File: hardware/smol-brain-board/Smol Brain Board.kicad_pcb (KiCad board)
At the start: 2 copper layers, 44.8 x 52.6 mm, 59 parts, among them J1 USB4085-GF-A, J3 CAN_DBG, J6 Smol_Brain_Board, J7 PROGRAM, U1 ESP32-S3-WROOM-1-N8, U3 SN65HVD231D

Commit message: fix: Corrected DRC settings
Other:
- rule pad_to_mask_clearance: 0.1016 -> 0.038

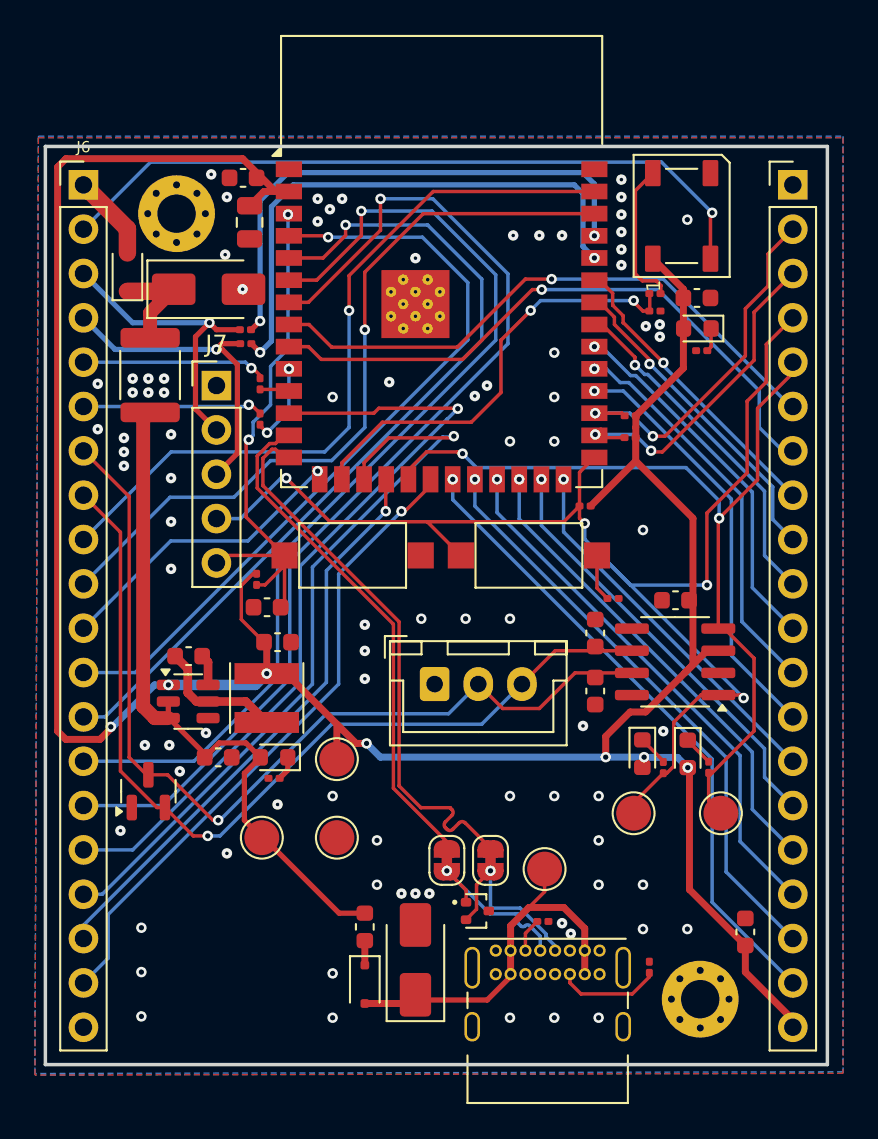
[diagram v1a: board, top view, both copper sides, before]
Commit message: Added real world components and finalised PCB, ready for manufacturing
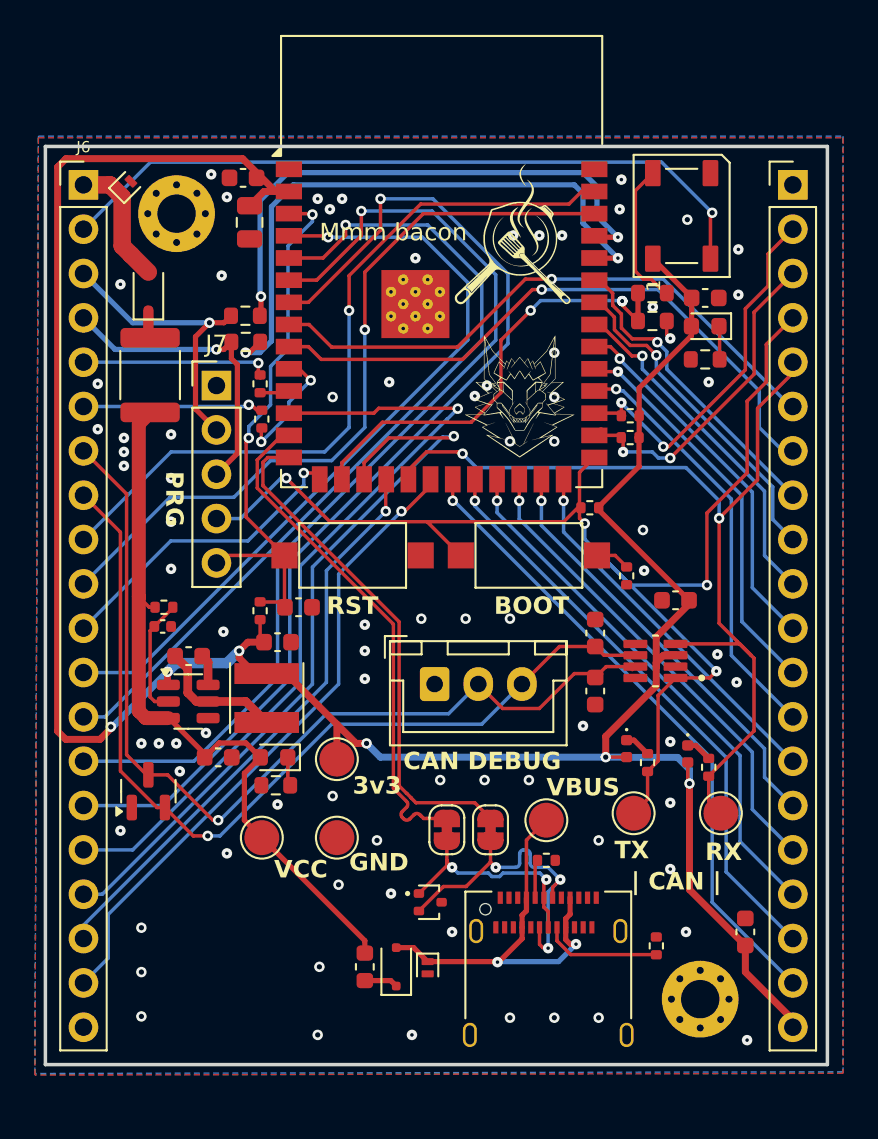
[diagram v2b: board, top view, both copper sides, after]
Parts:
- removed D5: SMBJ26A, Diode_SMD:D_SMA
- removed U3: SN65HVD231D, Package_SO:SOIC-8_3.9x4.9mm_P1.27mm
- added C12: 0.1uF, Capacitor_SMD:C_0402_1005Metric, F.Cu at (132.7, 106.3)
- added D7: PESD1, Diode_SMD:D_SOD-882, F.Cu at (130.7, 81.0)
- added R10: 10k, Resistor_SMD:R_0402_1005Metric, F.Cu at (132.8, 105.2)
- added U2: TCAN3414, Library:TCAN3414, F.Cu at (160.9, 108.3)
- C9: value Capacitor 1u 25V 0603 -> Capacitor 1u 25V
- CRX1, CTX1: footprint LED_SMD:LED_0603_1608Metric -> LED_SMD:LED_0402_1005Metric
- D2: value SMBJ5.0A-TR -> PESD1; footprint Diode_SMD:D_SMA -> Diode_SMD:D_SOD-882
- J1: value USB4085-GF-A -> USB_C_Receptacle; footprint Connector_USB:USB_C_Receptacle_GCT_USB4085 -> Connector_USB:USB_C_Receptacle_Amphenol_12401610E4-2A
- R1, R3: value Resistor 4.7k 0603 -> 4.7k; footprint Resistor_SMD:R_0201_0603Metric -> Resistor_SMD:R_0402_1005Metric
- R12, R14: value Resistor 1k 0603 -> 1k; footprint Resistor_SMD:R_0201_0603Metric -> Resistor_SMD:R_0402_1005Metric
- R13: value Resistor 100R 0603 -> 100R; footprint Resistor_SMD:R_0201_0603Metric -> Resistor_SMD:R_0402_1005Metric
- R15, R16, R5, R7, R8, R9: footprint Resistor_SMD:R_0201_0603Metric -> Resistor_SMD:R_0603_1608Metric
- R17, R18, R19: footprint Resistor_SMD:R_0201_0603Metric -> Resistor_SMD:R_0402_1005Metric
- R2, R4: value Resistor 5.1k 0603 -> Resistor 5.1k; footprint Resistor_SMD:R_0201_0603Metric -> Resistor_SMD:R_0402_1005Metric
- R6: value Resistor 10k 0603 -> 10k; footprint Resistor_SMD:R_0201_0603Metric -> Resistor_SMD:R_0402_1005Metric
- moved J1 3.61 mm to (154.8, 126.9)
- moved R4 3.51 mm to (154.7, 119.7)
- moved VBUS1 2.80 mm to (154.7, 117.4)
- moved D6 2.75 mm to (148.1, 122.1)
- moved F2 2.29 mm to (144.3, 125.8)
- moved D4 2.06 mm to (146.1, 125.8), turned to 90 degrees
- moved R6 1.81 mm to (138.3, 105.4), turned to 90 degrees
- moved C9 1.80 mm to (140.5, 105.2), turned to 0 degrees
- moved JP1 1.75 mm to (149.0, 118.0)
- moved JP2 1.75 mm to (151.5, 118.0)
- moved D1 1.63 mm to (131.9, 87.1)
- moved R13 1.52 mm to (159.3, 103.4), turned to -90 degrees
- moved R2 1.29 mm to (161.0, 124.6)
- moved R12 0.94 mm to (160.5, 114.1)
- moved CTX1 0.94 mm to (159.3, 113.3)
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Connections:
- J1 pad A8: (no net) -> unconnected-(J1-SBU1-PadA8)
- J1 pad B6: (no net) -> /USB_D_P
- J1 pad B7: (no net) -> /USB_D_N
- J1 pad B8: (no net) -> unconnected-(J1-SBU2-PadB8)
- VR1 pad 2: Net-(VIN_IND1-A) -> Net-(VR1-EN)
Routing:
- net /USB_D_N: track 10.4 -> 19.7 mm, vias 1 -> 3
- net Net-(VR1-EN): track 0.00 -> 7.25 mm
- net Net-(D1-K): track 6.04 -> 1.56 mm
- net /CAN_RX: track 51.3 -> 55.6 mm
- net Net-(U1-RXD0): track 31.9 -> 35.0 mm
- net /uC_USB_D_N: track 33.0 -> 30.0 mm
- net 3V3: track 156.6 -> 153.8 mm, vias 7 -> 6
- net /USB_D_P: track 10.4 -> 13.0 mm, vias 1 -> 2
- net VIN: track 4.94 -> 7.43 mm
- net Net-(U1-IO17): track 4.80 -> 7.17 mm
- net Net-(VIN_IND1-A): track 40.0 -> 41.8 mm
- net /CAN_TX: track 78.4 -> 76.7 mm
- net /RST: track 31.1 -> 32.6 mm
- net GND: track 0.00 -> 1.22 mm, vias 85 -> 79
- net VBUS: track 22.5 -> 23.6 mm, vias 0 -> 2
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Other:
- board text added: "BOOT"
- board text added: "CAN DEBUG"
- board text added: "Mmm bacon"
- board text added: "PRG"
- board text added: "RST"
- board text added: "VBUS"
- board text added: "VCC"
- board text added: "| CAN |"

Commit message: Fixed footprint mismatch
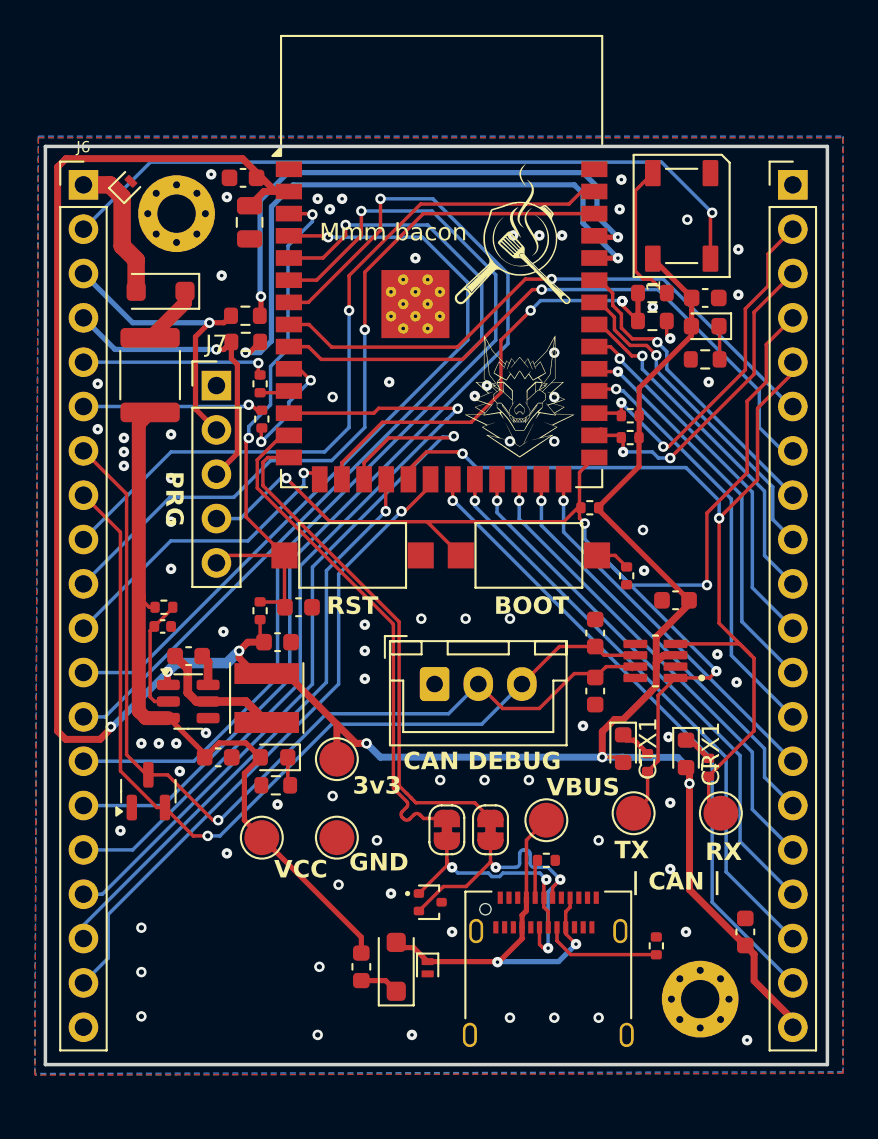
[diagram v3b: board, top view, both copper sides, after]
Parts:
- CRX1, CTX1: footprint LED_SMD:LED_0402_1005Metric -> LED_SMD:LED_0603_1608Metric
- D1, D4: footprint Diode_SMD:D_SOD-323F -> Diode_SMD:D_SOD-123F
- moved D1 0.70 mm to (132.6, 87.1), turned to 180 degrees
- moved CTX1 0.20 mm to (159.1, 113.3)
- moved F2 0.20 mm to (144.1, 125.8)
- moved CRX1 0.10 mm to (162.7, 113.6)
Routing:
- net Net-(D1-K): track 1.56 -> 3.49 mm
- net VIN: track 7.43 -> 8.24 mm
- net GND: vias 79 -> 78
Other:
- rule pad_to_mask_clearance: 0.038 -> 0
- board text added: "MRB JCN"
- board text removed: "JCN MRB"
